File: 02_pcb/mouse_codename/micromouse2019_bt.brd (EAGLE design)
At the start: 13 x 17.6 mm, 2 parts, among them U1 SPBT2632C2A.AT2

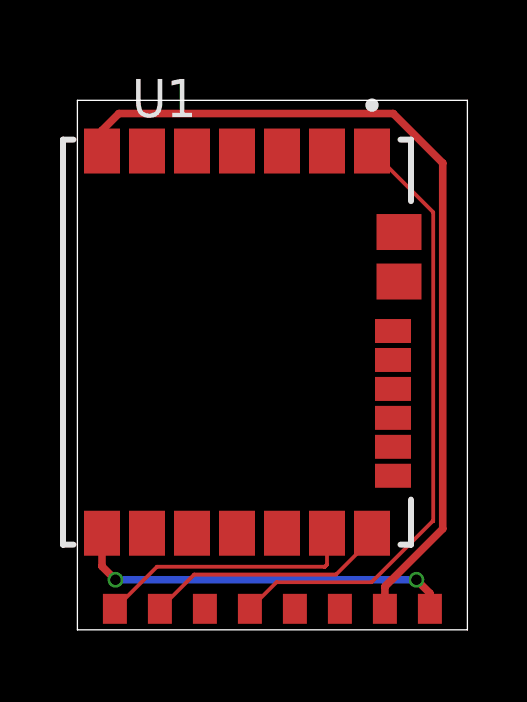
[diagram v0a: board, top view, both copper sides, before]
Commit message: bt_port tx rx changed
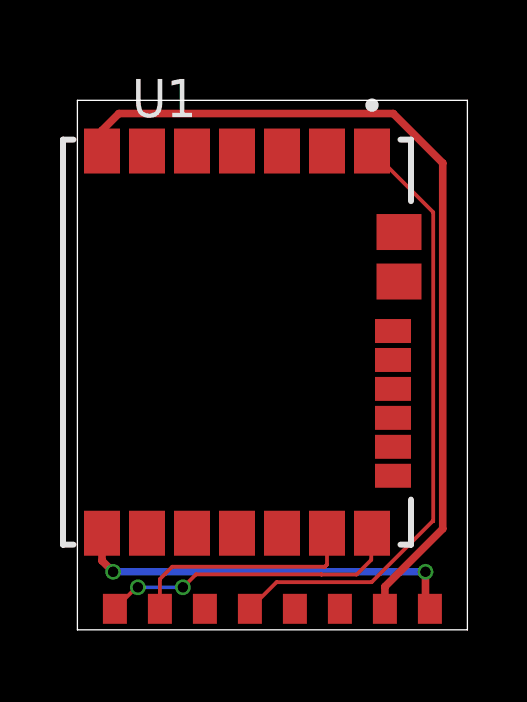
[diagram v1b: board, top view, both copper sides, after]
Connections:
- net BT_RX: now also PORT1.P9; no longer PORT1.P8
- net BT_TX: now also PORT1.P8; no longer PORT1.P9
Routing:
- net BT_TX: track 8.22 -> 10.3 mm, vias 0 -> 2
- net BT_RX: track 8.73 -> 7.81 mm
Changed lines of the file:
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@@
 <setting verticaltext="up"/>
 </settings>
-<grid distance="1" unitdist="mm" unit="mm" style="lines" multiple="1" display="yes" altdistance="5" altunitdist="mil" altunit="mil"/>
+<grid distance="5" unitdist="mil" unit="mil" style="lines" multiple="1" display="yes" altdistance="5" altunitdist="mil" altunit="mil"/>
 <layers>
 <layer number="1" name="Top" color="4" fill="1" visible="yes" active="yes"/>
@@
 <contactref element="U1" pad="8"/>
 <contactref element="PORT1" pad="P15"/>
-<wire x1="1.82" y1="4.57" x2="1.82" y2="3.466" width="0.254" layer="1"/>
-<wire x1="1.82" y1="3.466" x2="2.268" y2="3.018" width="0.254" layer="1"/>
-<via x="2.268" y="3.018" extent="1-16" drill="0.35"/>
-<wire x1="2.268" y1="3.018" x2="12.301" y2="3.018" width="0.254" layer="16"/>
-<via x="12.301" y="3.018" extent="1-16" drill="0.35"/>
-<wire x1="12.301" y1="3.018" x2="12.75" y2="2.569" width="0.254" layer="1"/>
-<wire x1="12.75" y1="2.569" x2="12.75" y2="2.05" width="0.254" layer="1"/>
+<wire x1="1.82" y1="4.57" x2="1.82" y2="3.653" width="0.254" layer="1"/>
+<wire x1="1.82" y1="3.653" x2="2.189" y2="3.284" width="0.254" layer="1"/>
+<via x="2.189" y="3.284" extent="1-16" drill="0.35"/>
+<wire x1="2.189" y1="3.284" x2="12.603" y2="3.284" width="0.254" layer="16"/>
+<via x="12.603" y="3.284" extent="1-16" drill="0.35"/>
+<wire x1="12.603" y1="3.284" x2="12.603" y2="2.197" width="0.254" layer="1"/>
+<wire x1="12.603" y1="2.197" x2="12.75" y2="2.05" width="0.254" layer="1"/>
 </signal>
 <signal name="GND">
@@
 <signal name="BT_TX">
 <contactref element="U1" pad="14"/>
-<contactref element="PORT1" pad="P9"/>
 <wire x1="10.82" y1="4.57" x2="10.82" y2="4.391" width="0.127" layer="1"/>
-<wire x1="9.622" y1="3.193" x2="10.82" y2="4.391" width="0.127" layer="1"/>
-<wire x1="3.75" y1="2.05" x2="4.893" y2="3.193" width="0.127" layer="1"/>
-<wire x1="4.893" y1="3.193" x2="9.622" y2="3.193" width="0.127" layer="1"/>
+<contactref element="PORT1" pad="P8"/>
+<wire x1="10.82" y1="4.57" x2="10.795" y2="4.545" width="0.127" layer="1"/>
+<wire x1="10.795" y1="4.545" x2="10.795" y2="3.683" width="0.127" layer="1"/>
+<wire x1="9.1357875" y1="3.193" x2="9.1297875" y2="3.199" width="0.127" layer="1"/>
+<wire x1="9.1297875" y1="3.199" x2="4.953" y2="3.199" width="0.127" layer="1"/>
+<wire x1="10.795" y1="3.683" x2="10.305" y2="3.193" width="0.127" layer="1"/>
+<wire x1="10.305" y1="3.193" x2="9.1357875" y2="3.193" width="0.127" layer="1"/>
+<wire x1="4.953" y1="3.199" x2="4.5215" y2="2.7675" width="0.127" layer="1"/>
+<wire x1="4.5215" y1="2.7675" x2="4.5166625" y2="2.7675" width="0.127" layer="1"/>
+<via x="4.5166625" y="2.7675" extent="1-16" drill="0.35"/>
+<wire x1="4.5166625" y1="2.7675" x2="3.0166625" y2="2.7675" width="0.127" layer="16"/>
+<via x="3.0166625" y="2.7675" extent="1-16" drill="0.35"/>
+<wire x1="3.0166625" y1="2.7675" x2="2.9675" y2="2.7675" width="0.127" layer="1"/>
+<wire x1="2.9675" y1="2.7675" x2="2.25" y2="2.05" width="0.127" layer="1"/>
 </signal>
 <signal name="STATUS">
@@
 <signal name="BT_RX">
 <contactref element="U1" pad="13"/>
-<contactref element="PORT1" pad="P8"/>
 <wire x1="9.32" y1="4.57" x2="9.32" y2="3.526" width="0.127" layer="1"/>
 <wire x1="9.241" y1="3.447" x2="9.247" y2="3.453" width="0.127" layer="1"/>
 <wire x1="9.247" y1="3.453" x2="9.32" y2="3.526" width="0.127" layer="1"/>
-<wire x1="2.25" y1="2.05" x2="3.653" y2="3.453" width="0.127" layer="1"/>
-<wire x1="3.653" y1="3.453" x2="9.247" y2="3.453" width="0.127" layer="1"/>
+<wire x1="9.247" y1="3.453" x2="4.161" y2="3.453" width="0.127" layer="1"/>
+<contactref element="PORT1" pad="P9"/>
+<wire x1="4.161" y1="3.453" x2="3.75" y2="3.042" width="0.127" layer="1"/>
+<wire x1="3.75" y1="3.042" x2="3.75" y2="2.05" width="0.127" layer="1"/>
 </signal>
 </signals>

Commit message: module pcbs updated
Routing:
- net GND: track 28.6 -> 5.53 mm, vias 0 -> 4
- added copper zone on layer 16, net GND
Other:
- board size 13 x 17.6 mm -> 13 x 17.8 mm
- board text added: "copper free zone"
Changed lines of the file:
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@@
 <setting verticaltext="up"/>
 </settings>
-<grid distance="5" unitdist="mil" unit="mil" style="lines" multiple="1" display="yes" altdistance="5" altunitdist="mil" altunit="mil"/>
+<grid distance="3.93700787" unitdist="mil" unit="mil" style="lines" multiple="1" display="yes" altdistance="1" altunitdist="mil" altunit="mil"/>
 <layers>
 <layer number="1" name="Top" color="4" fill="1" visible="yes" active="yes"/>
@@
 <plain>
 <wire x1="1" y1="1.35" x2="14" y2="1.35" width="0" layer="20"/>
-<wire x1="14" y1="1.35" x2="14" y2="19" width="0" layer="20"/>
-<wire x1="14" y1="19" x2="1" y2="19" width="0" layer="20"/>
-<wire x1="1" y1="19" x2="1" y2="1.35" width="0" layer="20"/>
+<wire x1="14" y1="1.35" x2="14" y2="19.1" width="0" layer="20"/>
+<wire x1="14" y1="19.1" x2="1" y2="19.1" width="0" layer="20"/>
+<wire x1="1" y1="19.1" x2="1" y2="1.35" width="0" layer="20"/>
 <dimension x1="14" y1="19" x2="1" y2="19" x3="7.5" y3="25" textsize="1.778" layer="47"/>
 <dimension x1="14" y1="1.35" x2="14" y2="19" x3="22" y3="10.175" textsize="1.778" layer="47"/>
+<rectangle x1="0.508" y1="10.795" x2="2.286" y2="15.367" layer="51"/>
+<wire x1="8.5" y1="18" x2="8.5" y2="5.5" width="0.1524" layer="52"/>
+<wire x1="8.5" y1="5.5" x2="0.5" y2="5.5" width="0.1524" layer="52"/>
+<text x="4" y="7" size="0.8" layer="51" rot="R90">copper free zone</text>
+<wire x1="8.5" y1="18" x2="0.5" y2="18" width="0.1524" layer="52"/>
 </plain>
 <attributes>
@@
 <attribute name="MF" value="STMicroelectronics" x="-0.03" y="-11.92" size="1.778" layer="27" rot="R270" display="off"/>
 <attribute name="MP" value="SPBT2632C2A.AT2" x="-0.03" y="-11.92" size="1.778" layer="27" rot="R270" display="off"/>
-<attribute name="NAME" x="2.819140625" y="18.44185" size="1.270309375" layer="25"/>
 <attribute name="PACKAGE" value="Module STMicroelectronics" x="-0.03" y="-11.92" size="1.778" layer="27" rot="R270" display="off"/>
 <attribute name="PRICE" value="None" x="-0.03" y="-11.92" size="1.778" layer="27" rot="R270" display="off"/>
-<attribute name="VALUE" x="7.8611" y="6.019590625" size="0.762" layer="27" rot="R90"/>
+<attribute name="VALUE" x="9.8611" y="6.519590625" size="0.762" layer="25" rot="R90"/>
 </element>
 </elements>
@@
 <contactref element="U1" pad="8"/>
 <contactref element="PORT1" pad="P15"/>
-<wire x1="1.82" y1="4.57" x2="1.82" y2="3.653" width="0.254" layer="1"/>
-<wire x1="1.82" y1="3.653" x2="2.189" y2="3.284" width="0.254" layer="1"/>
-<via x="2.189" y="3.284" extent="1-16" drill="0.35"/>
-<wire x1="2.189" y1="3.284" x2="12.603" y2="3.284" width="0.254" layer="16"/>
-<via x="12.603" y="3.284" extent="1-16" drill="0.35"/>
-<wire x1="12.603" y1="3.284" x2="12.603" y2="2.197" width="0.254" layer="1"/>
-<wire x1="12.603" y1="2.197" x2="12.75" y2="2.05" width="0.254" layer="1"/>
+<via x="2.2278" y="3.3828" extent="1-16" drill="0.3" diameter="0.6"/>
+<wire x1="12.75" y1="2.05" x2="12.843" y2="2.143" width="0.254" layer="1"/>
+<wire x1="1.82" y1="4.57" x2="1.82" y2="3.7906" width="0.2032" layer="1"/>
+<wire x1="1.82" y1="3.7906" x2="2.2278" y2="3.3828" width="0.2032" layer="1"/>
+<wire x1="2.2278" y1="3.3828" x2="12.7462" y2="3.3828" width="0.2032" layer="16"/>
+<wire x1="12.7462" y1="3.3828" x2="12.827" y2="3.302" width="0.2032" layer="16"/>
+<via x="12.827" y="3.302" extent="1-16" drill="0.3" diameter="0.6"/>
+<wire x1="12.827" y1="3.302" x2="12.827" y2="2.159" width="0.2032" layer="1"/>
+<wire x1="12.827" y1="2.159" x2="12.843" y2="2.143" width="0.2032" layer="1"/>
 </signal>
 <signal name="GND">
 <contactref element="U1" pad="7"/>
 <contactref element="PORT1" pad="P14"/>
-<wire x1="1.82" y1="17.31" x2="1.82" y2="17.997" width="0.254" layer="1"/>
-<wire x1="1.82" y1="17.997" x2="2.383" y2="18.56" width="0.254" layer="1"/>
-<wire x1="2.383" y1="18.56" x2="11.527" y2="18.56" width="0.254" layer="1"/>
-<wire x1="11.527" y1="18.56" x2="13.178" y2="16.909" width="0.254" layer="1"/>
-<wire x1="13.178" y1="16.909" x2="13.178" y2="4.717" width="0.254" layer="1"/>
-<wire x1="13.178" y1="4.717" x2="11.25" y2="2.789" width="0.254" layer="1"/>
-<wire x1="11.25" y1="2.789" x2="11.25" y2="2.05" width="0.254" layer="1"/>
+<wire x1="13.178" y1="4.59" x2="11.25" y2="2.662" width="0.3048" layer="1"/>
+<wire x1="11.25" y1="2.662" x2="11.25" y2="2.05" width="0.3048" layer="1"/>
+<polygon width="0.1524" layer="16">
+<vertex x="1" y="19"/>
+<vertex x="1" y="18"/>
+<vertex x="8.5" y="18"/>
+<vertex x="8.5" y="5.5"/>
+<vertex x="1" y="5.5"/>
+<vertex x="1" y="2.5"/>
+<vertex x="14" y="2.5"/>
+<vertex x="14" y="19"/>
+</polygon>
+<via x="13.208" y="4.572" extent="1-16" drill="0.3" diameter="0.6"/>
+<wire x1="13.208" y1="4.572" x2="13.196" y2="4.572" width="0.1524" layer="1"/>
+<wire x1="13.196" y1="4.572" x2="13.178" y2="4.59" width="0.1524" layer="1"/>
+<via x="12.7" y="4.064" extent="1-16" drill="0.3" diameter="0.6"/>
+<via x="1.905" y="18.542" extent="1-16" drill="0.3" diameter="0.6"/>
+<via x="2.794" y="18.542" extent="1-16" drill="0.3" diameter="0.6"/>
+<wire x1="2.794" y1="18.542" x2="1.905" y2="18.542" width="0.3048" layer="1"/>
+<wire x1="1.905" y1="18.542" x2="1.905" y2="17.395" width="0.3048" layer="1"/>
+<wire x1="1.905" y1="17.395" x2="1.82" y2="17.31" width="0.4064" layer="1"/>
 </signal>
 <signal name="BT_TX">
 <contactref element="U1" pad="14"/>
-<wire x1="10.82" y1="4.57" x2="10.82" y2="4.391" width="0.127" layer="1"/>
 <contactref element="PORT1" pad="P8"/>
 <wire x1="10.82" y1="4.57" x2="10.795" y2="4.545" width="0.127" layer="1"/>
@@
 <wire x1="10.305" y1="3.193" x2="9.1357875" y2="3.193" width="0.127" layer="1"/>
 <wire x1="4.953" y1="3.199" x2="4.5215" y2="2.7675" width="0.127" layer="1"/>
-<wire x1="4.5215" y1="2.7675" x2="4.5166625" y2="2.7675" width="0.127" layer="1"/>
-<via x="4.5166625" y="2.7675" extent="1-16" drill="0.35"/>
-<wire x1="4.5166625" y1="2.7675" x2="3.0166625" y2="2.7675" width="0.127" layer="16"/>
-<via x="3.0166625" y="2.7675" extent="1-16" drill="0.35"/>
-<wire x1="3.0166625" y1="2.7675" x2="2.9675" y2="2.7675" width="0.127" layer="1"/>
+<wire x1="4.5215" y1="2.7675" x2="4.5223" y2="2.8402625" width="0.127" layer="1"/>
+<via x="4.5223" y="2.8402625" extent="1-16" drill="0.3" diameter="0.6"/>
+<wire x1="4.5223" y1="2.8402625" x2="2.9729" y2="2.8388625" width="0.127" layer="16"/>
+<via x="2.9729" y="2.8388625" extent="1-16" drill="0.3" diameter="0.6"/>
+<wire x1="2.9729" y1="2.8388625" x2="2.9675" y2="2.7675" width="0.127" layer="1"/>
 <wire x1="2.9675" y1="2.7675" x2="2.25" y2="2.05" width="0.127" layer="1"/>
 </signal>
@@
 <contactref element="U1" pad="13"/>
 <wire x1="9.32" y1="4.57" x2="9.32" y2="3.526" width="0.127" layer="1"/>
-<wire x1="9.241" y1="3.447" x2="9.247" y2="3.453" width="0.127" layer="1"/>
 <wire x1="9.247" y1="3.453" x2="9.32" y2="3.526" width="0.127" layer="1"/>
 <wire x1="9.247" y1="3.453" x2="4.161" y2="3.453" width="0.127" layer="1"/>

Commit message: minor board updates
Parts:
- moved PORT1 0.25 mm to (7.50, 1.80)
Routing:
- net GND: track 5.53 -> 6.99 mm
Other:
- board size 13 x 17.8 mm -> 13 x 18 mm
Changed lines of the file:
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@@
 <drawing>
 <settings>
-<setting alwaysvectorfont="no"/>
+<setting alwaysvectorfont="yes"/>
 <setting verticaltext="up"/>
 </settings>
-<grid distance="3.93700787" unitdist="mil" unit="mil" style="lines" multiple="1" display="yes" altdistance="1" altunitdist="mil" altunit="mil"/>
+<grid distance="1.96850394" unitdist="mil" unit="mil" style="lines" multiple="1" display="yes" altdistance="1" altunitdist="mil" altunit="mil"/>
 <layers>
 <layer number="1" name="Top" color="4" fill="1" visible="yes" active="yes"/>
@@
 <layer number="27" name="tValues" color="7" fill="1" visible="yes" active="yes"/>
 <layer number="28" name="bValues" color="7" fill="1" visible="yes" active="yes"/>
-<layer number="29" name="tStop" color="7" fill="3" visible="no" active="yes"/>
+<layer number="29" name="tStop" color="7" fill="3" visible="yes" active="yes"/>
 <layer number="30" name="bStop" color="7" fill="6" visible="no" active="yes"/>
 <layer number="31" name="tCream" color="7" fill="4" visible="no" active="yes"/>
@@
 <board>
 <plain>
-<wire x1="1" y1="1.35" x2="14" y2="1.35" width="0" layer="20"/>
-<wire x1="14" y1="1.35" x2="14" y2="19.1" width="0" layer="20"/>
+<wire x1="1" y1="1.1" x2="14" y2="1.1" width="0" layer="20"/>
+<wire x1="14" y1="1.1" x2="14" y2="19.1" width="0" layer="20"/>
 <wire x1="14" y1="19.1" x2="1" y2="19.1" width="0" layer="20"/>
-<wire x1="1" y1="19.1" x2="1" y2="1.35" width="0" layer="20"/>
+<wire x1="1" y1="19.1" x2="1" y2="1.1" width="0" layer="20"/>
 <dimension x1="14" y1="19" x2="1" y2="19" x3="7.5" y3="25" textsize="1.778" layer="47"/>
 <dimension x1="14" y1="1.35" x2="14" y2="19" x3="22" y3="10.175" textsize="1.778" layer="47"/>
@@
 </autorouter>
 <elements>
-<element name="PORT1" library="0-micromouse2019" package="BT_PORT_MODULE" package3d_urn="urn:adsk.eagle:package:9190656/1" value="PORT_BT_MODULE" x="7.5" y="2.05" smashed="yes">
-<attribute name="VALUE" x="1.75" y="0.518334375" size="0.7" layer="27"/>
+<element name="PORT1" library="0-micromouse2019" package="BT_PORT_MODULE" package3d_urn="urn:adsk.eagle:package:9190656/1" value="PORT_BT_MODULE" x="7.5" y="1.8" smashed="yes">
+<attribute name="VALUE" x="1.75" y="0.268334375" size="0.7" layer="27"/>
 </element>
 <element name="U1" library="0-micromouse2019" package="XCVR_SPBT2632C2A.AT2" value="SPBT2632C2A.AT2" x="6.32" y="10.94" smashed="yes" rot="R270">
@@
 <contactref element="PORT1" pad="P15"/>
 <via x="2.2278" y="3.3828" extent="1-16" drill="0.3" diameter="0.6"/>
-<wire x1="12.75" y1="2.05" x2="12.843" y2="2.143" width="0.254" layer="1"/>
 <wire x1="1.82" y1="4.57" x2="1.82" y2="3.7906" width="0.2032" layer="1"/>
 <wire x1="1.82" y1="3.7906" x2="2.2278" y2="3.3828" width="0.2032" layer="1"/>
-<wire x1="2.2278" y1="3.3828" x2="12.7462" y2="3.3828" width="0.2032" layer="16"/>
-<wire x1="12.7462" y1="3.3828" x2="12.827" y2="3.302" width="0.2032" layer="16"/>
-<via x="12.827" y="3.302" extent="1-16" drill="0.3" diameter="0.6"/>
-<wire x1="12.827" y1="3.302" x2="12.827" y2="2.159" width="0.2032" layer="1"/>
-<wire x1="12.827" y1="2.159" x2="12.843" y2="2.143" width="0.2032" layer="1"/>
+<wire x1="2.2278" y1="3.3828" x2="12.6462" y2="3.3828" width="0.2032" layer="16"/>
+<wire x1="12.6462" y1="3.3828" x2="13.027" y2="3.002" width="0.2032" layer="16"/>
+<via x="13.027" y="3.002" extent="1-16" drill="0.3" diameter="0.6"/>
+<wire x1="13.027" y1="3.002" x2="13.027" y2="2.327" width="0.2032" layer="1"/>
+<wire x1="12.75" y1="1.8" x2="13.027" y2="2.327" width="0.2032" layer="1"/>
 </signal>
 <signal name="GND">
@@
 <contactref element="PORT1" pad="P14"/>
 <wire x1="13.178" y1="4.59" x2="11.25" y2="2.662" width="0.3048" layer="1"/>
-<wire x1="11.25" y1="2.662" x2="11.25" y2="2.05" width="0.3048" layer="1"/>
-<polygon width="0.1524" layer="16">
+<wire x1="11.25" y1="2.662" x2="11.25" y2="1.8" width="0.3048" layer="1"/>
+<polygon width="0.1524" layer="16" isolate="0.254">
 <vertex x="1" y="19"/>
 <vertex x="1" y="18"/>
@@
 <vertex x="14" y="19"/>
 </polygon>
-<via x="13.208" y="4.572" extent="1-16" drill="0.3" diameter="0.6"/>
-<wire x1="13.208" y1="4.572" x2="13.196" y2="4.572" width="0.1524" layer="1"/>
-<wire x1="13.196" y1="4.572" x2="13.178" y2="4.59" width="0.1524" layer="1"/>
-<via x="12.7" y="4.064" extent="1-16" drill="0.3" diameter="0.6"/>
+<via x="13.158" y="5.822" extent="1-16" drill="0.3" diameter="0.6"/>
+<wire x1="13.158" y1="5.822" x2="13.178" y2="5.802" width="0.1524" layer="1"/>
+<wire x1="13.178" y1="5.802" x2="13.178" y2="4.59" width="0.3048" layer="1"/>
+<via x="13.2" y="4.664" extent="1-16" drill="0.3" diameter="0.6"/>
 <via x="1.905" y="18.542" extent="1-16" drill="0.3" diameter="0.6"/>
 <via x="2.794" y="18.542" extent="1-16" drill="0.3" diameter="0.6"/>
@@
 <wire x1="10.82" y1="4.57" x2="10.795" y2="4.545" width="0.127" layer="1"/>
 <wire x1="10.795" y1="4.545" x2="10.795" y2="3.683" width="0.127" layer="1"/>
-<wire x1="9.1357875" y1="3.193" x2="9.1297875" y2="3.199" width="0.127" layer="1"/>
-<wire x1="9.1297875" y1="3.199" x2="4.953" y2="3.199" width="0.127" layer="1"/>
-<wire x1="10.795" y1="3.683" x2="10.305" y2="3.193" width="0.127" layer="1"/>
-<wire x1="10.305" y1="3.193" x2="9.1357875" y2="3.193" width="0.127" layer="1"/>
-<wire x1="4.953" y1="3.199" x2="4.5215" y2="2.7675" width="0.127" layer="1"/>
-<wire x1="4.5215" y1="2.7675" x2="4.5223" y2="2.8402625" width="0.127" layer="1"/>
+<wire x1="10.155" y1="3.043" x2="4.797" y2="3.043" width="0.127" layer="1"/>
+<wire x1="10.795" y1="3.683" x2="10.155" y2="3.043" width="0.127" layer="1"/>
 <via x="4.5223" y="2.8402625" extent="1-16" drill="0.3" diameter="0.6"/>
 <wire x1="4.5223" y1="2.8402625" x2="2.9729" y2="2.8388625" width="0.127" layer="16"/>
 <via x="2.9729" y="2.8388625" extent="1-16" drill="0.3" diameter="0.6"/>
 <wire x1="2.9729" y1="2.8388625" x2="2.9675" y2="2.7675" width="0.127" layer="1"/>
-<wire x1="2.9675" y1="2.7675" x2="2.25" y2="2.05" width="0.127" layer="1"/>
+<wire x1="2.9675" y1="2.7675" x2="2.25" y2="1.8" width="0.127" layer="1"/>
+<wire x1="4.5223" y1="2.8402625" x2="4.5942625" y2="2.8402625" width="0.127" layer="1"/>
+<wire x1="4.5942625" y1="2.8402625" x2="4.797" y2="3.043" width="0.127" layer="1"/>
 </signal>
 <signal name="STATUS">
 <contactref element="U1" pad="1"/>
 <contactref element="PORT1" pad="P11"/>
-<wire x1="12.84040625" y1="4.971" x2="12.8605" y2="4.971" width="0.127" layer="1"/>
-<wire x1="10.80840625" y1="2.939" x2="12.84040625" y2="4.971" width="0.127" layer="1"/>
-<wire x1="12.8605" y1="4.971" x2="12.8605" y2="15.2695" width="0.127" layer="1"/>
-<wire x1="12.8605" y1="15.2695" x2="10.82" y2="17.31" width="0.127" layer="1"/>
-<wire x1="6.75" y1="2.05" x2="7.639" y2="2.939" width="0.127" layer="1"/>
-<wire x1="7.639" y1="2.939" x2="10.80840625" y2="2.939" width="0.127" layer="1"/>
+<wire x1="10.60840625" y1="2.739" x2="12.55" y2="4.68059375" width="0.127" layer="1"/>
+<wire x1="10.82" y1="17.31" x2="12.8605" y2="15.2695" width="0.127" layer="1"/>
+<wire x1="6.75" y1="1.8" x2="7.482896875" y2="2.739" width="0.127" layer="1"/>
+<wire x1="7.482896875" y1="2.739" x2="10.60840625" y2="2.739" width="0.127" layer="1"/>
+<wire x1="12.8605" y1="15.2695" x2="12.8605" y2="11.9605" width="0.127" layer="1"/>
+<wire x1="12.8605" y1="11.9605" x2="12.55" y2="11.65" width="0.127" layer="1"/>
+<wire x1="12.55" y1="11.65" x2="12.55" y2="4.68059375" width="0.127" layer="1"/>
 </signal>
 <signal name="BT_RX">
@@
 <contactref element="PORT1" pad="P9"/>
 <wire x1="4.161" y1="3.453" x2="3.75" y2="3.042" width="0.127" layer="1"/>
-<wire x1="3.75" y1="3.042" x2="3.75" y2="2.05" width="0.127" layer="1"/>
+<wire x1="3.75" y1="3.042" x2="3.75" y2="1.8" width="0.127" layer="1"/>
 </signal>
 </signals>
